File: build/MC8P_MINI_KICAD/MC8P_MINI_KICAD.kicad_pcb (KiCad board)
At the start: 2 copper layers, 139.2 x 67.5 mm, 29 parts, among them J1 AudioJack3, SW1 ASSIGN, SW2 ENTER, SW3 PREV, SW4 NEXT, U1 CD74HC4067M

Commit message: production files
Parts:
- removed the G*** at (106.0, 41.0)
- added G***: LOGO, MC8P_mini:collage_60mm_fmask, F.Cu at (129.8, 37.8)
- added G***: LOGO, MC8P_mini:collage_60mm_fmask, F.Cu at (64.5, 75.2)
- added G***: LOGO, MC8P_mini:church_30mm_fmask, F.Cu at (149.0, 41.2)
- added G***: LOGO, MC8P_mini:collage_60mm_fmask, F.Cu at (161.2, 91.0)
- added G***: LOGO, MC8P_mini:collage_60mm_fmask, F.Cu at (108.0, 39.9)
- added G***: LOGO, MC8P_mini:collage_60mm_fmask, F.Cu at (30.6, 91.0)
- added G***: LOGO, MC8P_mini:collage_60mm_fmask, B.Cu at (160.9, 91.4)
- added G***: LOGO, MC8P_mini:collage_30mm_fmask, B.Cu at (30.8, 90.8)
- added R3: 10k_0402, PCM_4ms_Resistor:R_0603, F.Cu at (145.4, 65.6)
- added R4: 10k_0402, PCM_4ms_Resistor:R_0603, F.Cu at (152.4, 65.6)
- added R5: 10k_0402, PCM_4ms_Resistor:R_0603, F.Cu at (152.4, 84.6)
- added R6: 10k_0402, PCM_4ms_Resistor:R_0603, F.Cu at (145.4, 84.6)
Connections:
- SW1 pad 1: ASSIGN -> 5V
- SW1 pad 2: GND -> ASSIGN
- SW2 pad 1: ENTER -> 5V
- SW2 pad 2: GND -> ENTER
- SW3 pad 1: PREV -> 5V
- SW3 pad 2: GND -> PREV
- SW4 pad 1: NEXT -> 5V
- SW4 pad 2: GND -> NEXT
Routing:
- net 5V: track 273.6 -> 388.3 mm
- net GND: track 39.7 -> 19.2 mm, vias 6 -> 10
- net 3v3: track 129.3 -> 120.6 mm
- net NEXT: track 153.0 -> 161.2 mm
- net ASSIGN: track 107.9 -> 114.8 mm
- net PREV: track 163.7 -> 170.3 mm
- net ENTER: track 124.5 -> 129.0 mm

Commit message: PCB & Schematic Updated
Added pull up resistors with jumpers to work with Arduino nano r4
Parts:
- added JP1: SolderJumper_2_Open, Jumper:SolderJumper-2_P1.3mm_Open_RoundedPad1.0x1.5mm, B.Cu at (144.0, 37.0)
- added JP2: SolderJumper_2_Open, Jumper:SolderJumper-2_P1.3mm_Open_RoundedPad1.0x1.5mm, B.Cu at (143.8, 40.0)
- added R8: 10k_0402, PCM_4ms_Resistor:R_0603, F.Cu at (140.0, 37.0)
- added R9: 10k_0402, PCM_4ms_Resistor:R_0603, F.Cu at (140.0, 40.0)
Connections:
- A1 pad 17: 3v3 -> unconnected-(A1-3V3-Pad17)
- Brd1 pad 2: 3v3 -> 5V
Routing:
- net 3v3: track 120.6 -> 0.00 mm
- net 5V: track 388.3 -> 433.5 mm
- net SDA: track 210.3 -> 223.3 mm
- net SCL: track 201.1 -> 209.6 mm
- net Net-(JP1-A): track 0.00 -> 2.50 mm, vias 0 -> 1
- net Net-(JP2-A): track 0.00 -> 2.35 mm, vias 0 -> 1
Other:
- board text added: "short the jumpers if using nano r4"

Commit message: PCB updated
updated back side to indicate when jumper wires are used
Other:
- board text added: "connect jumpers if OLED has SSD1315 IC"
- board text removed: "short the jumpers if using nano r4"

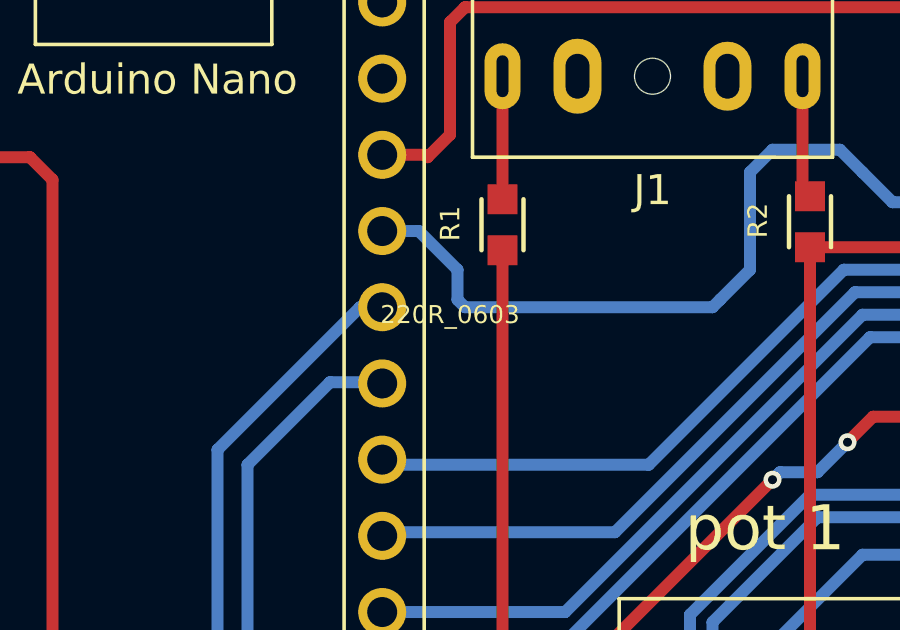
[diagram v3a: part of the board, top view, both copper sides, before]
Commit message: added ProMicro version
Created ProMicro version for USB MIDI support
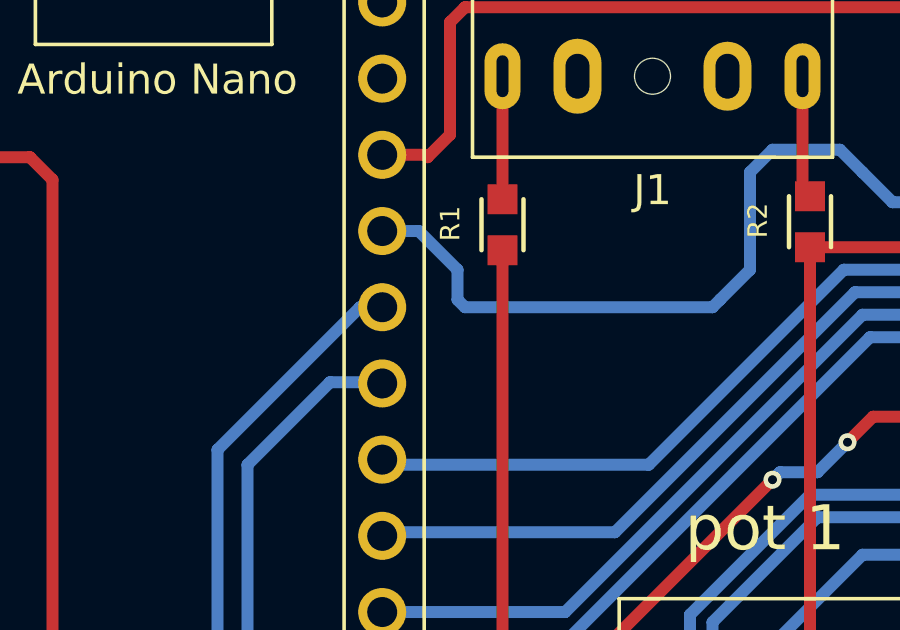
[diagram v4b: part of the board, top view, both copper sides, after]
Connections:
- R8 pad 1: 5V -> Net-(JP2-A)
- R8 pad 2: Net-(JP1-A) -> 5V
- R9 pad 1: 5V -> Net-(JP1-A)
- R9 pad 2: Net-(JP2-A) -> 5V
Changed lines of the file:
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@@
 			)
 		)
+		(property ki_fp_filters "R_*")
+		(sheetname "/")
+		(sheetfile "MC8P_MINI_KICAD.kicad_sch")
 		(attr smd)
 		(fp_line
@@
 			(size 1 1)
 			(layers "F.Cu" "F.Mask" "F.Paste")
-			(net 14 "5V")
+			(net 49 "Net-(JP1-A)")
 			(pintype "passive")
 		)
@@
 			(size 1 1)
 			(layers "F.Cu" "F.Mask" "F.Paste")
-			(net 50 "Net-(JP2-A)")
+			(net 14 "5V")
 			(pintype "passive")
 		)
@@
 		(sheetname "/")
 		(sheetfile "MC8P_MINI_KICAD.kicad_sch")
-		(attr through_hole exclude_from_pos_files exclude_from_bom dnp)
+		(attr through_hole exclude_from_pos_files)
 		(fp_line
 			(start 0.88 -2.38)
@@
 		(sheetname "/")
 		(sheetfile "MC8P_MINI_KICAD.kicad_sch")
-		(attr through_hole exclude_from_pos_files exclude_from_bom dnp)
+		(attr through_hole exclude_from_pos_files)
 		(fp_line
 			(start 0.88 -2.38)
@@
 		(sheetname "/")
 		(sheetfile "MC8P_MINI_KICAD.kicad_sch")
-		(attr through_hole exclude_from_pos_files exclude_from_bom dnp)
+		(attr through_hole exclude_from_pos_files)
 		(fp_line
 			(start 0.88 -2.38)
@@
 		(sheetname "/")
 		(sheetfile "MC8P_MINI_KICAD.kicad_sch")
-		(attr through_hole exclude_from_pos_files exclude_from_bom dnp)
+		(attr through_hole exclude_from_pos_files)
 		(fp_line
 			(start 0.88 -2.38)
@@
 		(sheetname "/")
 		(sheetfile "MC8P_MINI_KICAD.kicad_sch")
-		(attr through_hole exclude_from_pos_files exclude_from_bom dnp)
+		(attr through_hole exclude_from_pos_files)
 		(fp_line
 			(start 16.64 39.5)
@@
 		(sheetname "/")
 		(sheetfile "MC8P_MINI_KICAD.kicad_sch")
-		(attr through_hole exclude_from_pos_files exclude_from_bom dnp)
+		(attr through_hole exclude_from_pos_files)
 		(fp_line
 			(start 0.88 -2.38)
@@
 			)
 		)
+		(property ki_fp_filters "R_*")
+		(sheetname "/")
+		(sheetfile "MC8P_MINI_KICAD.kicad_sch")
 		(attr smd)
 		(fp_line
@@
 			(size 1 1)
 			(layers "F.Cu" "F.Mask" "F.Paste")
-			(net 14 "5V")
+			(net 50 "Net-(JP2-A)")
 			(pintype "passive")
 		)
@@
 			(size 1 1)
 			(layers "F.Cu" "F.Mask" "F.Paste")
-			(net 49 "Net-(JP1-A)")
+			(net 14 "5V")
 			(pintype "passive")
 		)
@@
 		(sheetname "/")
 		(sheetfile "MC8P_MINI_KICAD.kicad_sch")
-		(attr through_hole exclude_from_pos_files exclude_from_bom dnp)
+		(attr through_hole exclude_from_pos_files)
 		(fp_line
 			(start -13.4 -12.3)
@@
 		(sheetname "/")
 		(sheetfile "MC8P_MINI_KICAD.kicad_sch")
-		(attr through_hole exclude_from_pos_files exclude_from_bom dnp)
+		(attr through_hole exclude_from_pos_files)
 		(fp_line
 			(start 6 3.3)
@@
 		(sheetname "/")
 		(sheetfile "MC8P_MINI_KICAD.kicad_sch")
-		(attr through_hole exclude_from_pos_files exclude_from_bom dnp)
+		(attr through_hole exclude_from_pos_files)
 		(fp_line
 			(start 0.88 -2.38)
@@
 		(sheetname "/")
 		(sheetfile "MC8P_MINI_KICAD.kicad_sch")
-		(attr through_hole exclude_from_pos_files exclude_from_bom dnp)
+		(attr through_hole exclude_from_pos_files)
 		(fp_line
 			(start 0.88 -2.38)
@@
 		(sheetname "/")
 		(sheetfile "MC8P_MINI_KICAD.kicad_sch")
-		(attr through_hole exclude_from_pos_files exclude_from_bom dnp)
+		(attr through_hole exclude_from_pos_files)
 		(fp_line
 			(start 0.88 -2.38)
@@
 			(at 3 1.75 0)
 			(layer "F.SilkS")
+			(hide yes)
 			(effects
 				(font
@@
 		(sheetfile "MC8P_MINI_KICAD.kicad_sch")
 		(zone_connect 1)
-		(attr exclude_from_pos_files exclude_from_bom dnp allow_soldermask_bridges)
+		(attr exclude_from_pos_files exclude_from_bom allow_soldermask_bridges)
 		(fp_rect
 			(start -0.15 0.75)
@@
 		(sheetfile "MC8P_MINI_KICAD.kicad_sch")
 		(zone_connect 1)
-		(attr exclude_from_pos_files exclude_from_bom dnp allow_soldermask_bridges)
+		(attr exclude_from_pos_files exclude_from_bom allow_soldermask_bridges)
 		(fp_rect
 			(start -0.15 0.75)

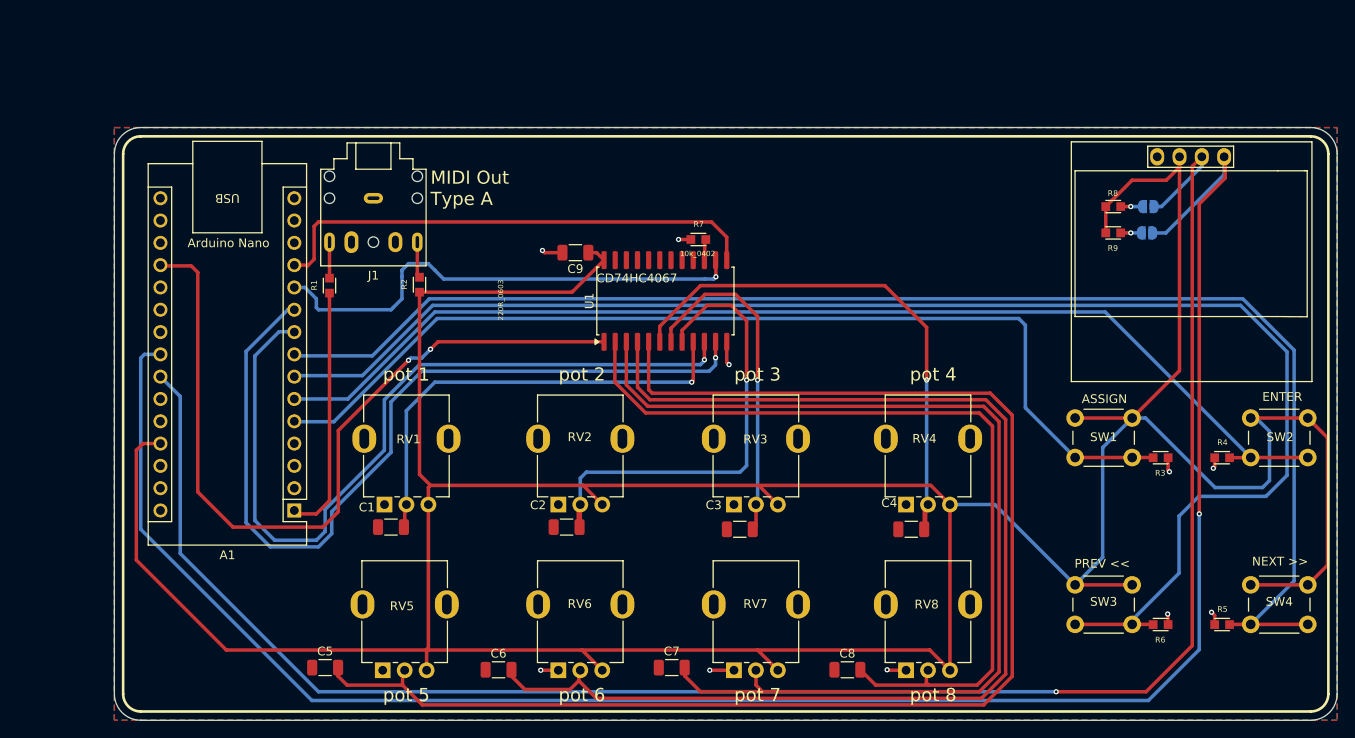
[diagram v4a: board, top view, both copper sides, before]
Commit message: PCV Rev2
replaced Nano version with Pro Micro
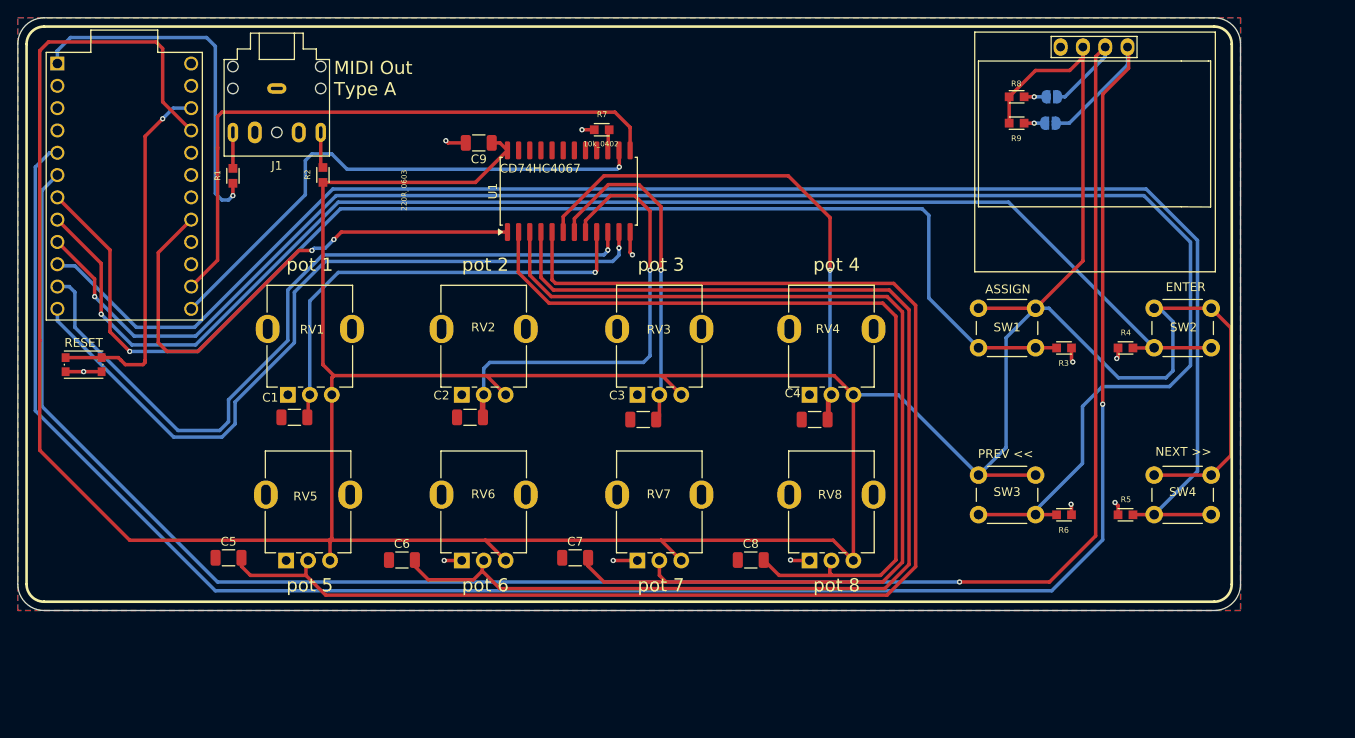
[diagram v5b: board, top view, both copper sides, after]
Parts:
- removed A1: Arduino_Nano_v2.x, Module:Arduino_Nano
- removed the G*** at (129.8, 37.8)
- removed the G*** at (64.5, 75.2)
- removed the G*** at (161.2, 91.0)
- removed the G*** at (108.0, 39.9)
- removed the G*** at (30.6, 91.0)
- removed the G*** at (160.9, 91.4)
- added G***: LOGO, MC8P_mini:collage_60mm_fmask, F.Cu at (19.6, 78.5)
- added G***: LOGO, MC8P_mini:collage_60mm_fmask, F.Cu at (53.5, 62.8)
- added G***: LOGO, MC8P_mini:collage_60mm_fmask, F.Cu at (97.0, 27.4)
- added G***: LOGO, MC8P_mini:collage_60mm_fmask, F.Cu at (150.2, 78.5)
- added G***: LOGO, MC8P_mini:collage_60mm_fmask, B.Cu at (149.9, 78.9)
- added SW5: RESET, Button_Switch_SMD:SW_Push_1P1T_NO_CK_KMR2, F.Cu at (22.8, 55.0)
- added U2: ProMicro, promicro:ProMicro, F.Cu at (27.4, 34.7)
- moved Brd1 16.7 mm to (137.6, 29.4)
- moved C1 16.7 mm to (46.8, 61.0)
- moved C2 16.7 mm to (66.8, 61.0)
- moved C3 16.7 mm to (86.5, 61.2)
- moved C4 16.7 mm to (106.0, 61.2)
- moved C5 16.7 mm to (39.2, 77.0)
- moved C6 16.7 mm to (59.0, 77.2)
- moved C7 16.7 mm to (78.7, 77.0)
- moved C8 16.7 mm to (98.7, 77.2)
- moved C9 16.7 mm to (67.8, 29.8)
- moved G*** 16.7 mm to (138.0, 28.8)
- moved G*** 16.7 mm to (19.8, 78.2)
- moved J1 16.7 mm to (44.8, 23.6)
- moved JP1 16.7 mm to (133.0, 24.5)
- moved JP2 16.7 mm to (132.8, 27.5)
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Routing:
- net 5V: track 433.5 -> 488.9 mm
- net RESET: track 0.00 -> 41.8 mm, vias 0 -> 1
- net ASSIGN: track 114.8 -> 145.3 mm, vias 0 -> 1
- net SIG: track 91.7 -> 61.4 mm
- net ENTER: track 129.0 -> 156.9 mm, vias 0 -> 1
- net PREV: track 170.3 -> 195.2 mm, vias 0 -> 1
- net NEXT: track 161.2 -> 184.0 mm
- net S3: track 56.9 -> 71.4 mm
- net TX: track 28.4 -> 41.2 mm, vias 0 -> 1
- net SCL: track 209.6 -> 222.1 mm
- net S1: track 97.6 -> 86.8 mm
- net SDA: track 223.3 -> 233.7 mm
- net S0: track 92.0 -> 87.3 mm
- net S2: track 56.5 -> 61.1 mm
- net GND: track 19.2 -> 23.3 mm, vias 10 -> 11
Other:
- board text removed: "Arduino Nano"
